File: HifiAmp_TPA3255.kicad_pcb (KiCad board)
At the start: 4 copper layers, 200 x 150 mm, 124 parts, among them J1 PVDD 48V IN — NEEDS_DATA, J2 RCA L SE, J3 RCA R SE, J301 SPK_L, J302 SPK_R, J4 VOLUME_REMOTE, Q301 IPP330P10NM, Q302 IXTK200N10L2, U1 LM5010ASD, U2 LM2940IMP-12/NOPB, U3 TLV1117-33IDCY, U4 OPA1612AIDR, U5 OPA1612AIDR, U6 TPA3255B, U7 TPS3802K33DCKR, U8 LM5069-2

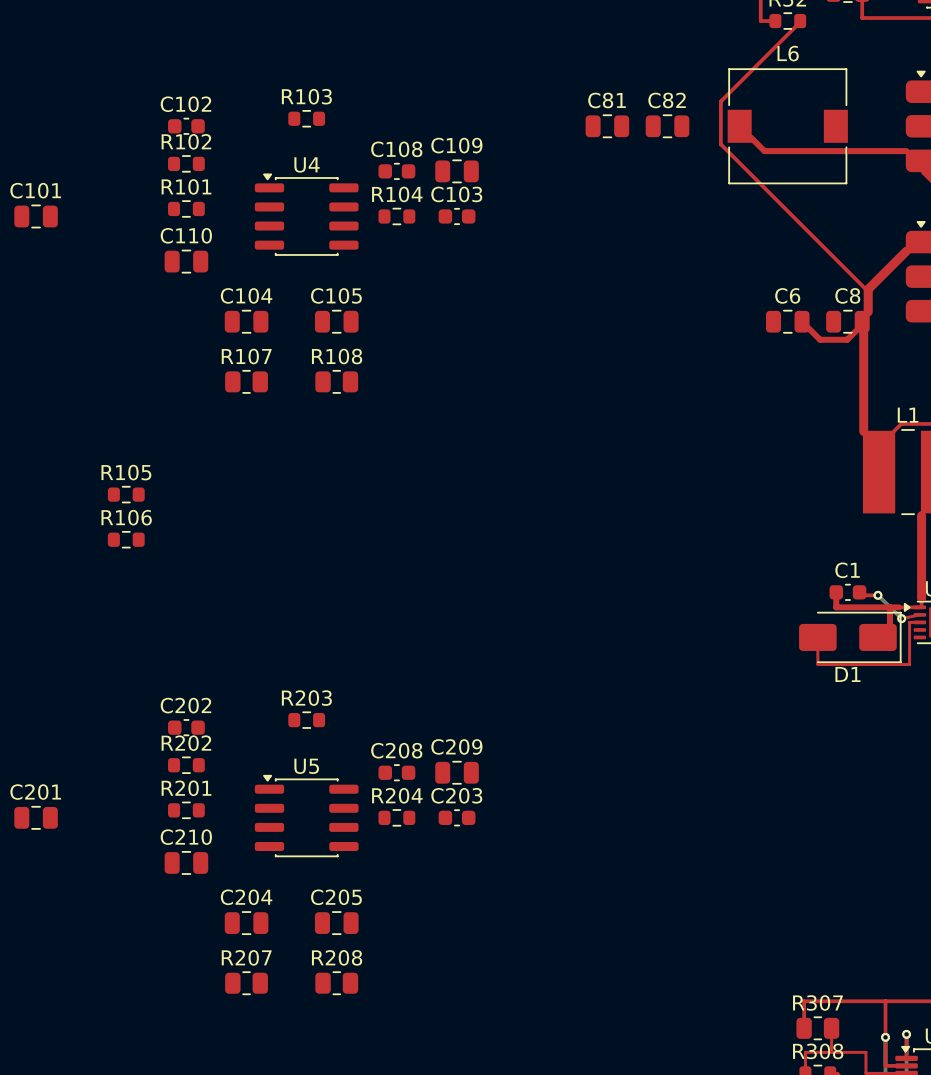
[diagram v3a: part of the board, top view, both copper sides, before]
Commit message: feat(f1.3-c): route the analog supplies with VMID equal on both channels
+12V-OA, VMID star (equal to 0.01 mm between U4 and U5), +/-VSE and AC nets.
Unconnected 147 -> 113, DRC silk-only, parity 3. F1.3-d now starts by moving
+/-VSE out of the PWR_OUT class.

Co-Authored-By: Claude Opus 5.5 <noreply@anthropic.com>
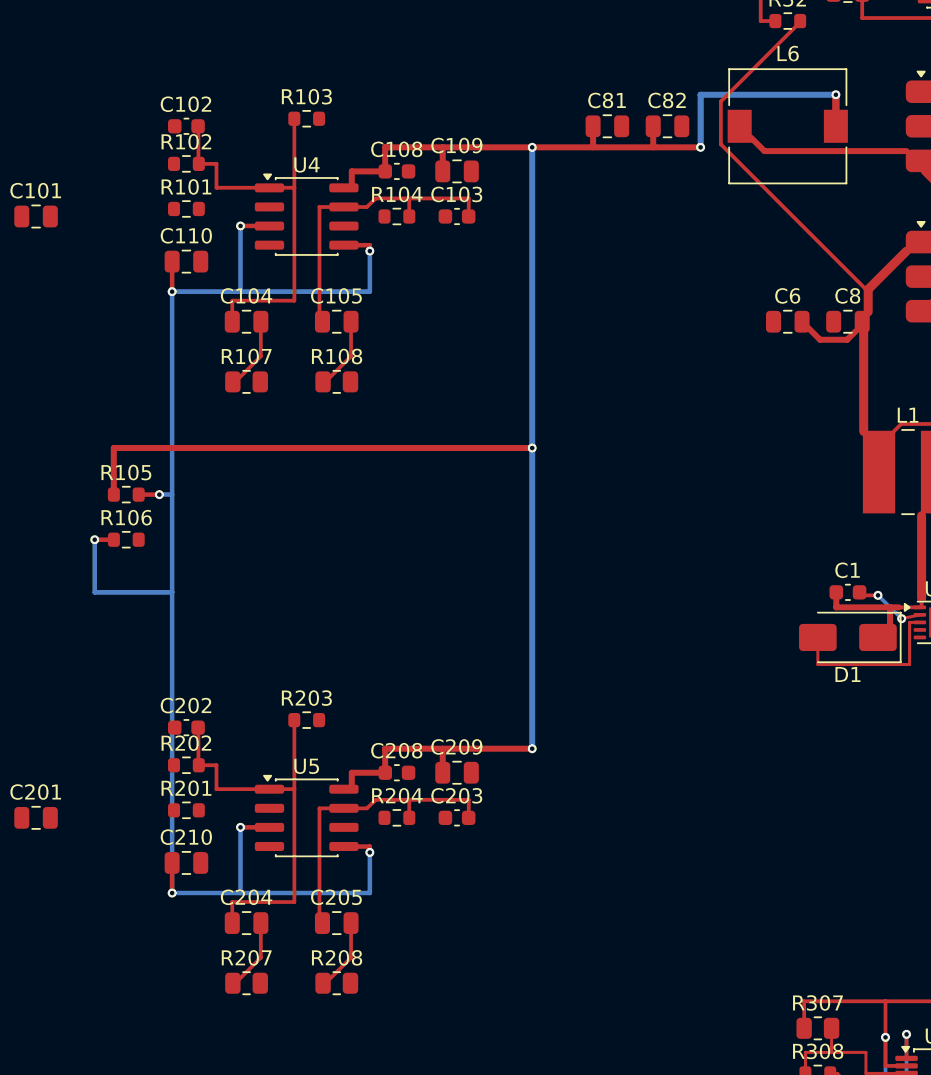
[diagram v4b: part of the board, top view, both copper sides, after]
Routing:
- net /+12V-OA: track 0.00 -> 129.6 mm, vias 0 -> 5
- net /VMID: track 0.00 -> 104.7 mm, vias 0 -> 8
- net /-VSE_R: track 0.00 -> 28.1 mm
- net /-VSE: track 0.00 -> 28.1 mm
- net /+VSE_R: track 0.00 -> 20.2 mm
- net /+VSE: track 0.00 -> 20.2 mm
- net /R_NEG_AC: track 0.00 -> 4.23 mm
- net /L_NEG_AC: track 0.00 -> 4.23 mm
- net /R_POS_AC: track 0.00 -> 4.23 mm
- net /L_POS_AC: track 0.00 -> 4.23 mm

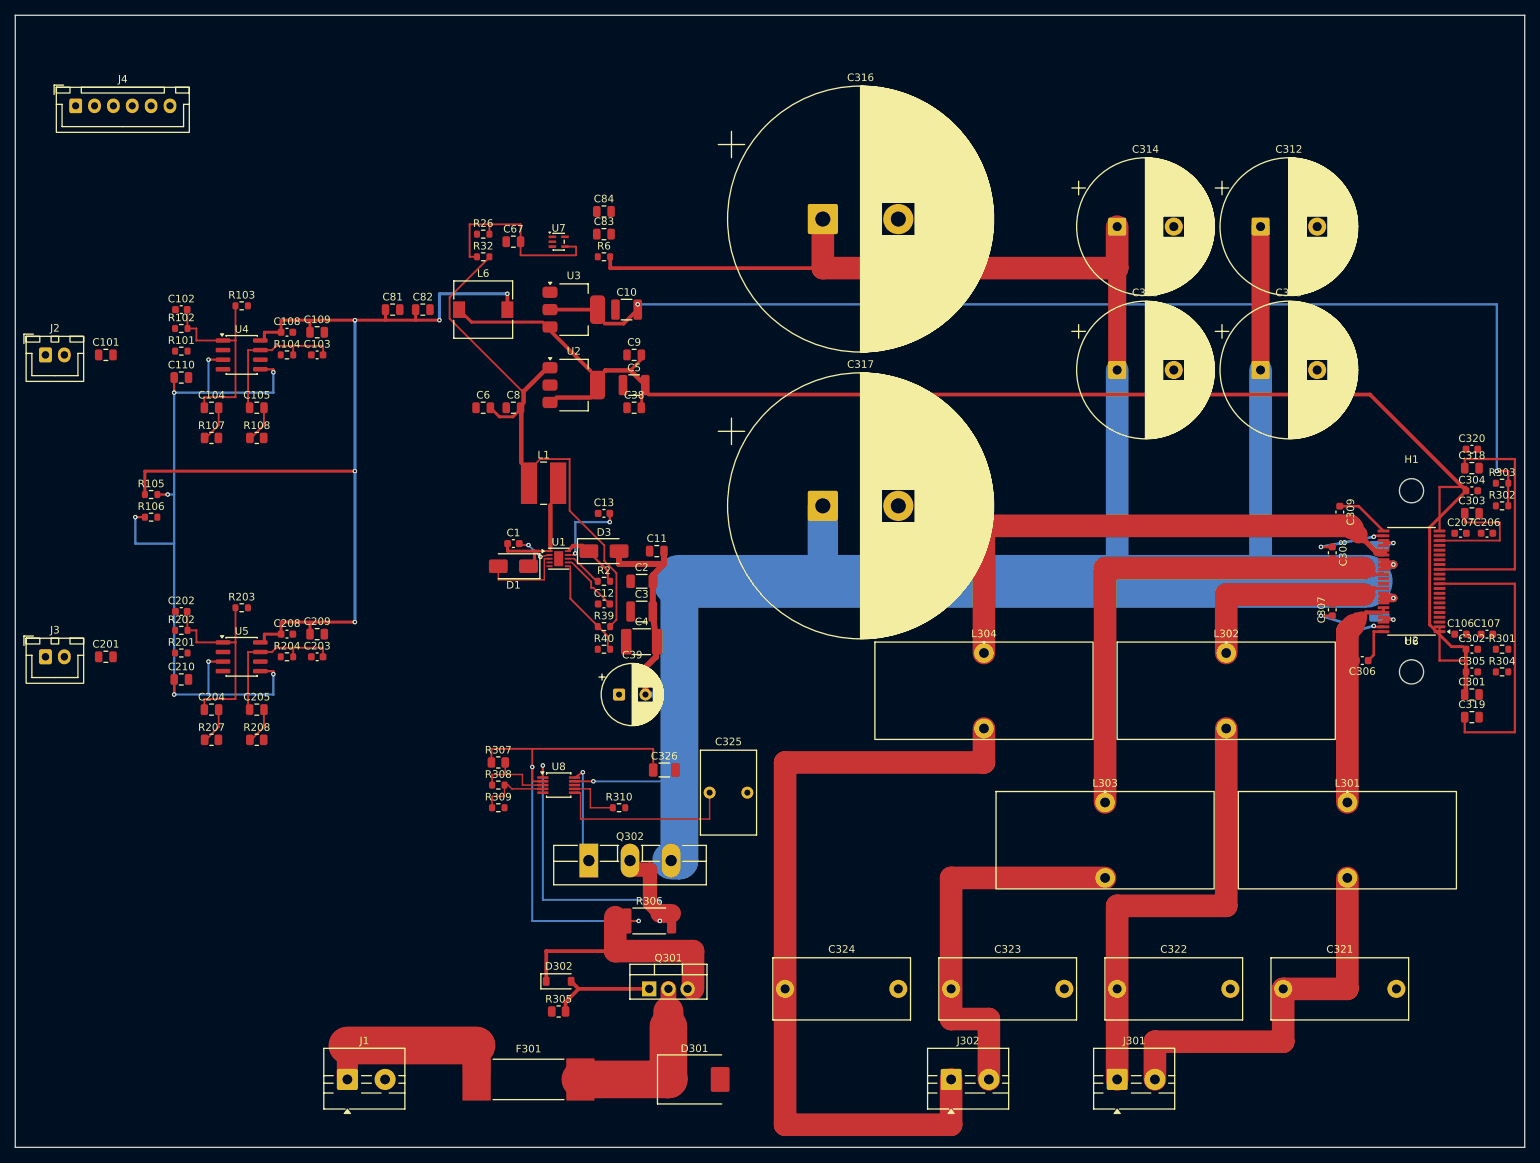
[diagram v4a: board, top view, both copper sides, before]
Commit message: feat(f1.3-d): route the analog signal path, move +/-VSE to the ANALOG class
INPUT pairs matched (0.45 / 0.00 mm), channels translated by 40 mm, 24.6 mm
from SW. Unconnected 113 -> 87, DRC silk-only, parity 3, prior copper
unchanged by UUID.

Co-Authored-By: Claude Opus 5.5 <noreply@anthropic.com>
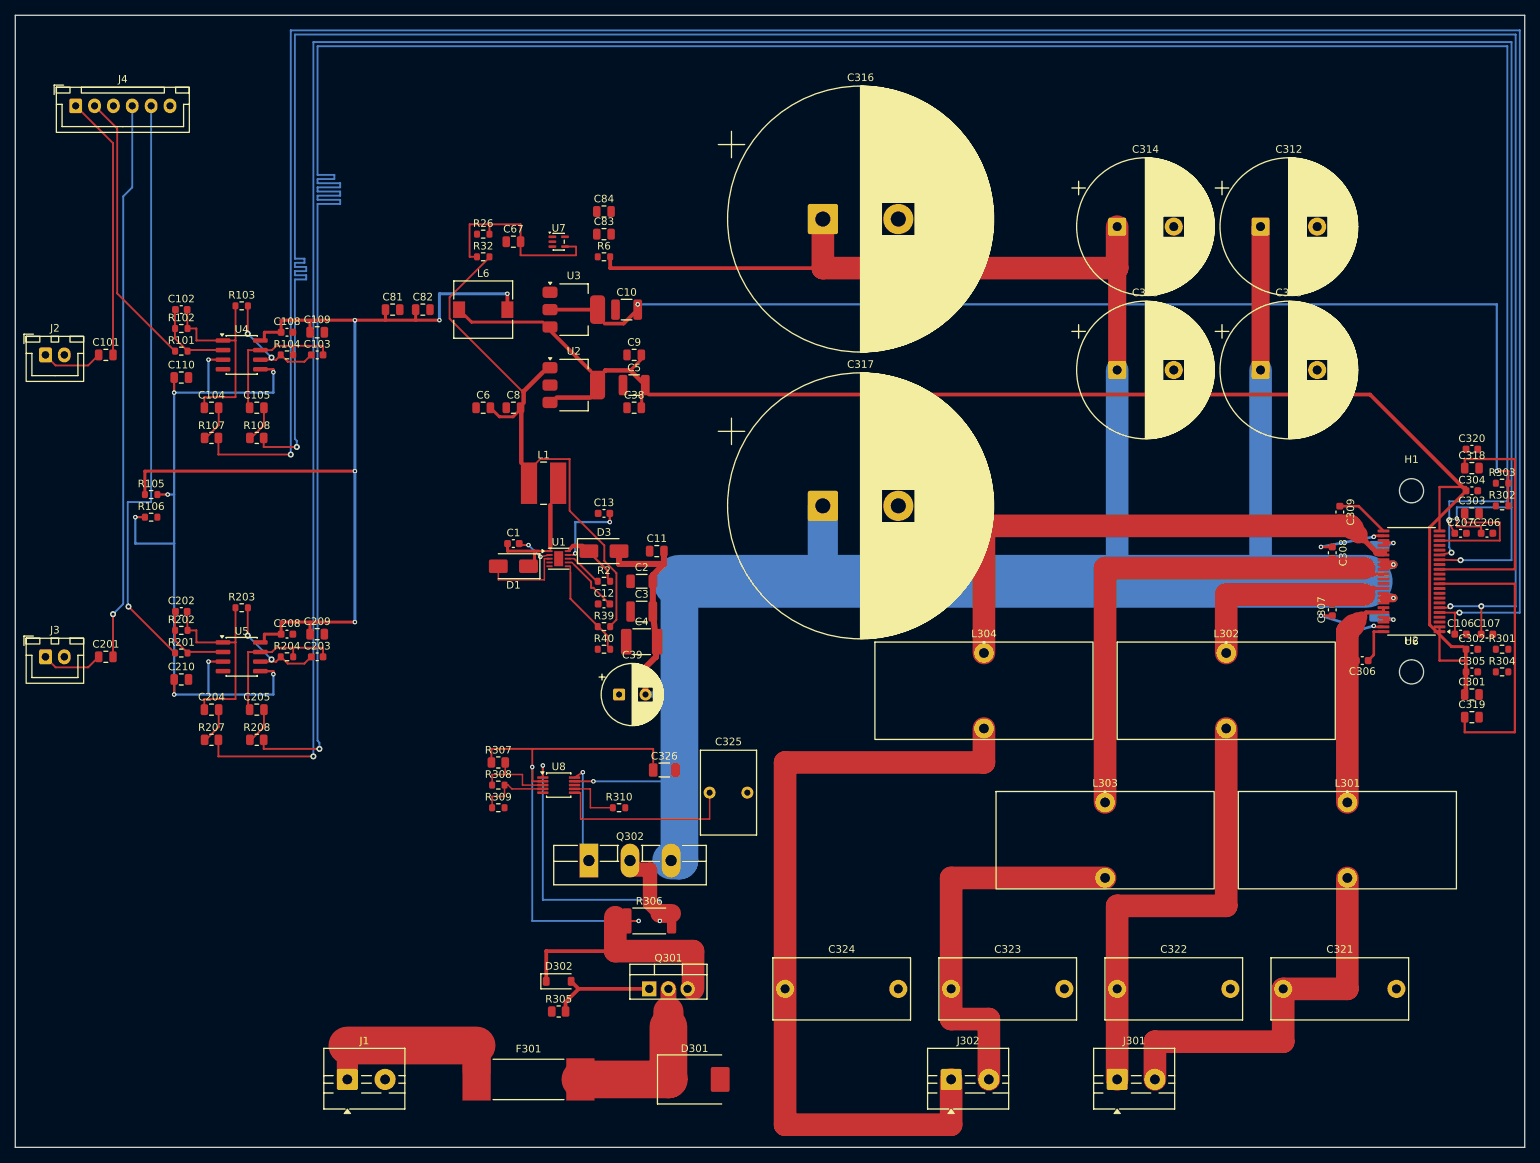
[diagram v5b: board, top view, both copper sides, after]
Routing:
- net /INPUT_D: track 0.00 -> 360.3 mm, vias 0 -> 3
- net /INPUT_C: track 0.00 -> 360.3 mm, vias 0 -> 3
- net /INPUT_A: track 0.00 -> 321.5 mm, vias 0 -> 2
- net /INPUT_B: track 0.00 -> 320.4 mm, vias 0 -> 3
- net /VOL_R: track 0.00 -> 78.2 mm, vias 0 -> 1
- net /VOL_R_IN: track 0.00 -> 74.1 mm, vias 0 -> 1
- net /VOL_L: track 0.00 -> 36.9 mm
- net /VOL_L_IN: track 0.00 -> 35.1 mm
- net /INV4_NEG: track 0.00 -> 16.3 mm, vias 0 -> 2
- net /INV2_NEG: track 0.00 -> 16.3 mm, vias 0 -> 2
- net /INV3_NEG: track 0.00 -> 11.2 mm
- net /INV1_NEG: track 0.00 -> 11.2 mm
- net /RCA_R: track 0.00 -> 8.24 mm
- net /RCA_L: track 0.00 -> 8.24 mm

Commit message: feat(f1.3-e): route the control nets, closing F1.3
Everything but GND is routed. Three INPUT vias near U6 shrunk to 0.6/0.3 to
free the control exits; INPUT_C/D stay matched to 0.10 mm. Unconnected
87 -> 78 (all GND), DRC silk-only, parity 3. F1.6 is moved ahead of F1.4.

Co-Authored-By: Claude Opus 5.5 <noreply@anthropic.com>
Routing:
- net /RESET: track 0.00 -> 142.2 mm, vias 0 -> 2
- net /C_START: track 0.00 -> 26.4 mm, vias 0 -> 2
- net /OC_ADJ: track 0.00 -> 14.2 mm
- net /FAULT: track 0.00 -> 13.8 mm
- net /FREQ_ADJ: track 0.00 -> 13.5 mm
- net /CLIP_OTW: track 0.00 -> 11.6 mm
- net /RESET-SW: track 0.00 -> 8.05 mm
- net /RESET_RC: track 0.00 -> 3.88 mm

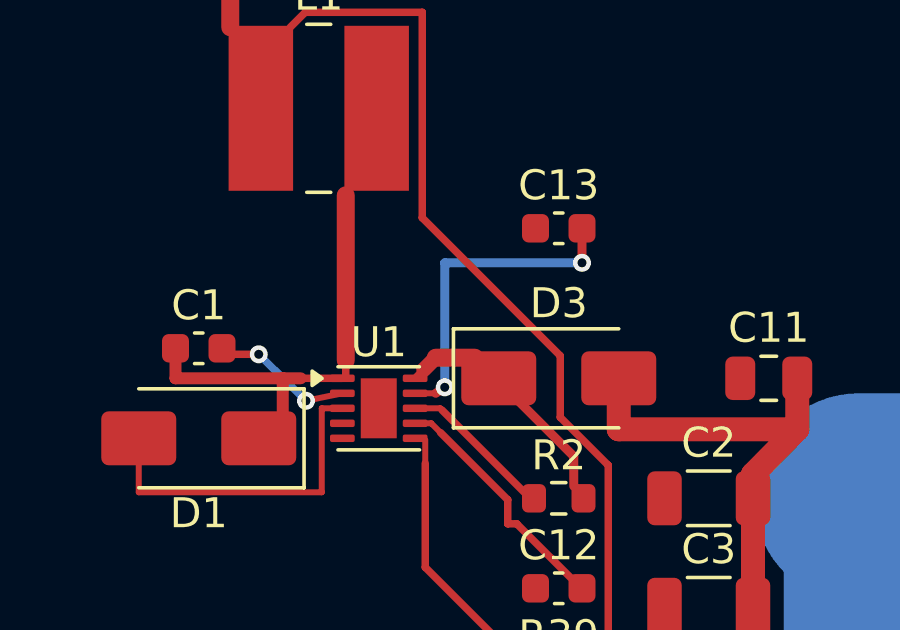
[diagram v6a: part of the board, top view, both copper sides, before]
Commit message: feat(f1.6): add the LM5010A input decoupling C327/C328 next to U1
The buck VIN had no local capacitor behind the series Schottky D3. Per
SNVS376F, 0.1 uF + 2.2 uF 100 V now sit at 1.3 mm of U1.10 with ground
straight onto the exposed pad. Parity 3, 78 GND left, ERC unchanged.

Co-Authored-By: Claude Opus 5.5 <noreply@anthropic.com>
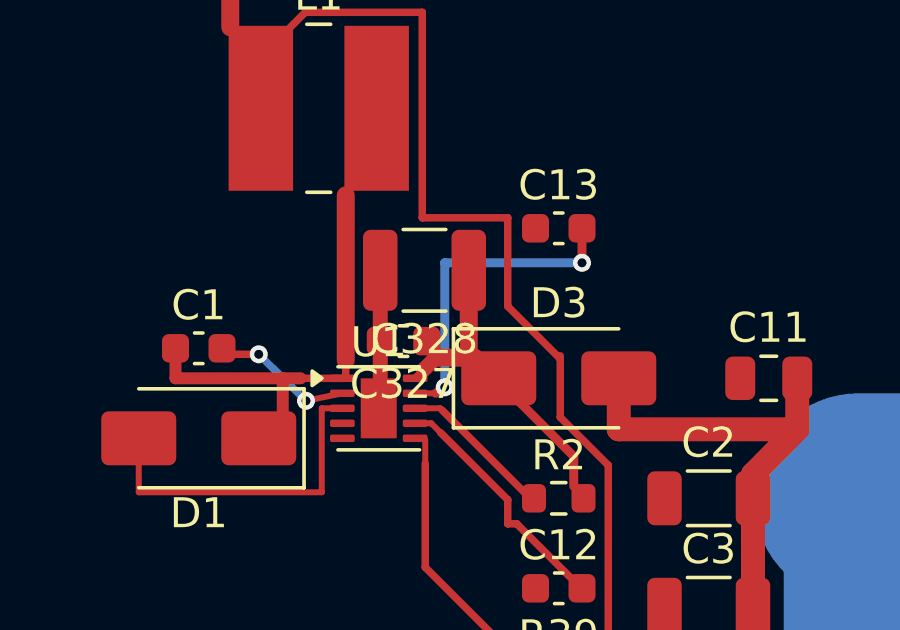
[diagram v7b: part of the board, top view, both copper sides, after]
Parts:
- added C327: 0.1uF/100V, Capacitor_SMD:C_0603_1608Metric, F.Cu at (172.8, 169.8)
- added C328: 2.2uF/100V, Capacitor_SMD:C_1210_3225Metric, F.Cu at (173.5, 167.4)
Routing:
- net /GND: track 6.37 -> 8.62 mm
- net /+15V: track 68.3 -> 70.1 mm
- net /BUCK_VIN: track 7.94 -> 9.50 mm

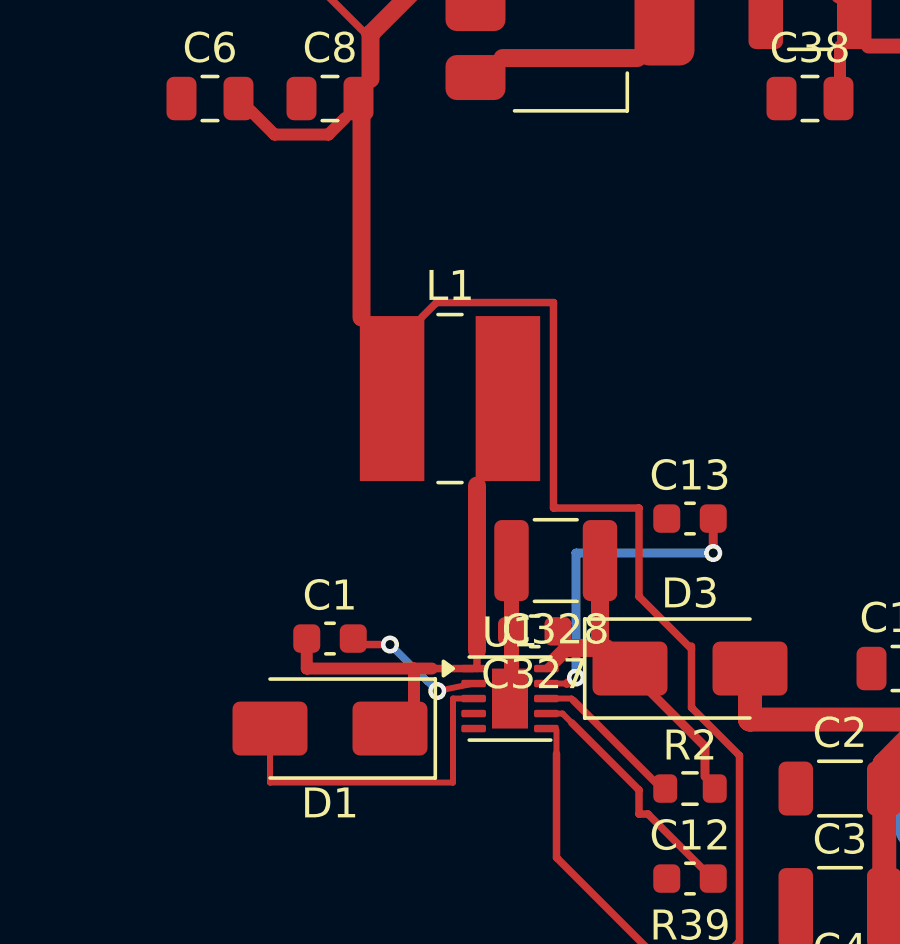
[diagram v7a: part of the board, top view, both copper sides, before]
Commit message: feat(f1.7): propagate the U1/L1 footprints to the PCB (F8)
Co-Authored-By: Claude Opus 5.5 <noreply@anthropic.com>
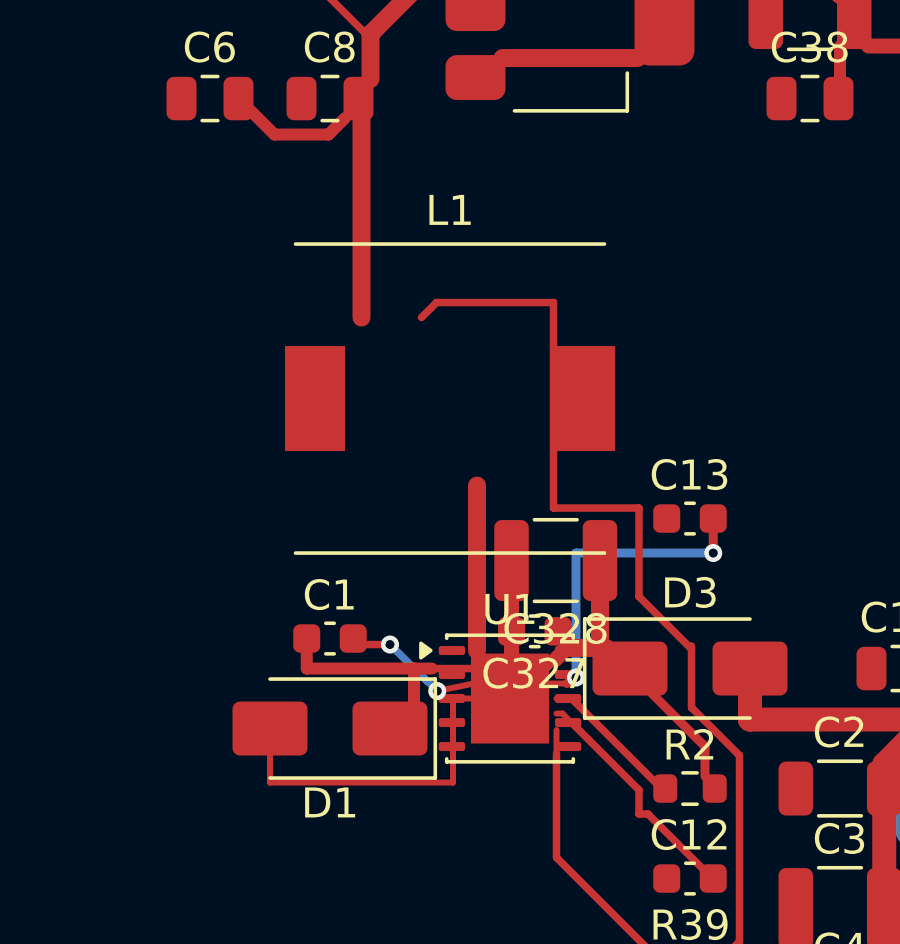
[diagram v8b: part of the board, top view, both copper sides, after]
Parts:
- L1: footprint Inductor_SMD:L_Wuerth_WE-PD2-Typ-MS -> HifiAmp_TPA3255_Local:L_Wuerth_WE-PD-1050_10x10x5mm
- U1: footprint Package_SON:WSON-10-1EP_2.5x2.5mm_P0.5mm_EP1.2x2mm -> Package_SON:WSON-10-1EP_4x4mm_P0.8mm_EP2.6x3mm
